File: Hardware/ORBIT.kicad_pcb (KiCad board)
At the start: 2 copper layers, 50 x 50 mm, 53 parts, among them J1 West Connector, J2 East Connector, U1 MCP73031, U10 8MHz, U11 30p, U12 30p, U13 22uF, U14 10uF, U15 TPS63802DLAR, U16 STM32F030C8Tx, U17 AT24C128C, U18 10p, U19 100n, U2 4u7, U20 4.7uF, U21 100nF, U22 CP2102-GMR, U23 1uF, U24 100nF, U3 100n, U4 100n, U5 100n, U6 100n, U7 4u7, U8 4u7, U9 100n

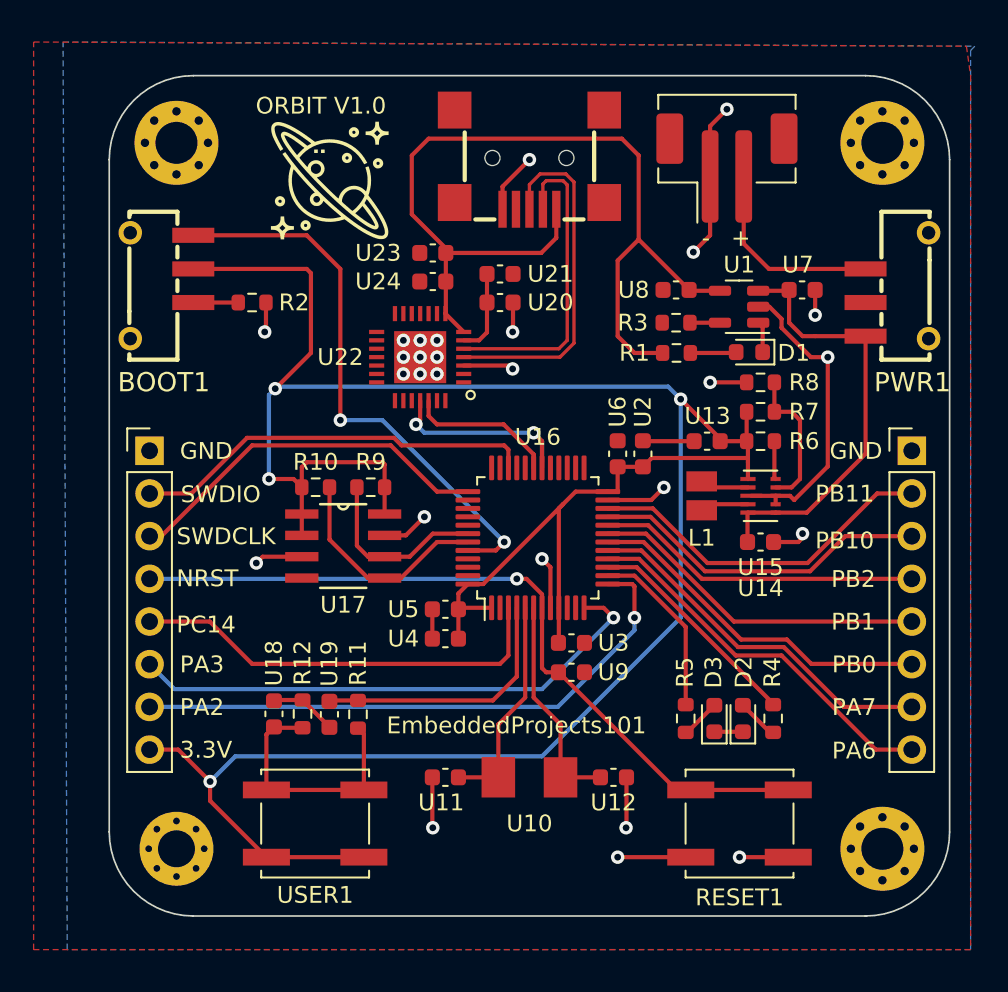
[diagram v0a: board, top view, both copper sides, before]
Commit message: all components in the final positioned
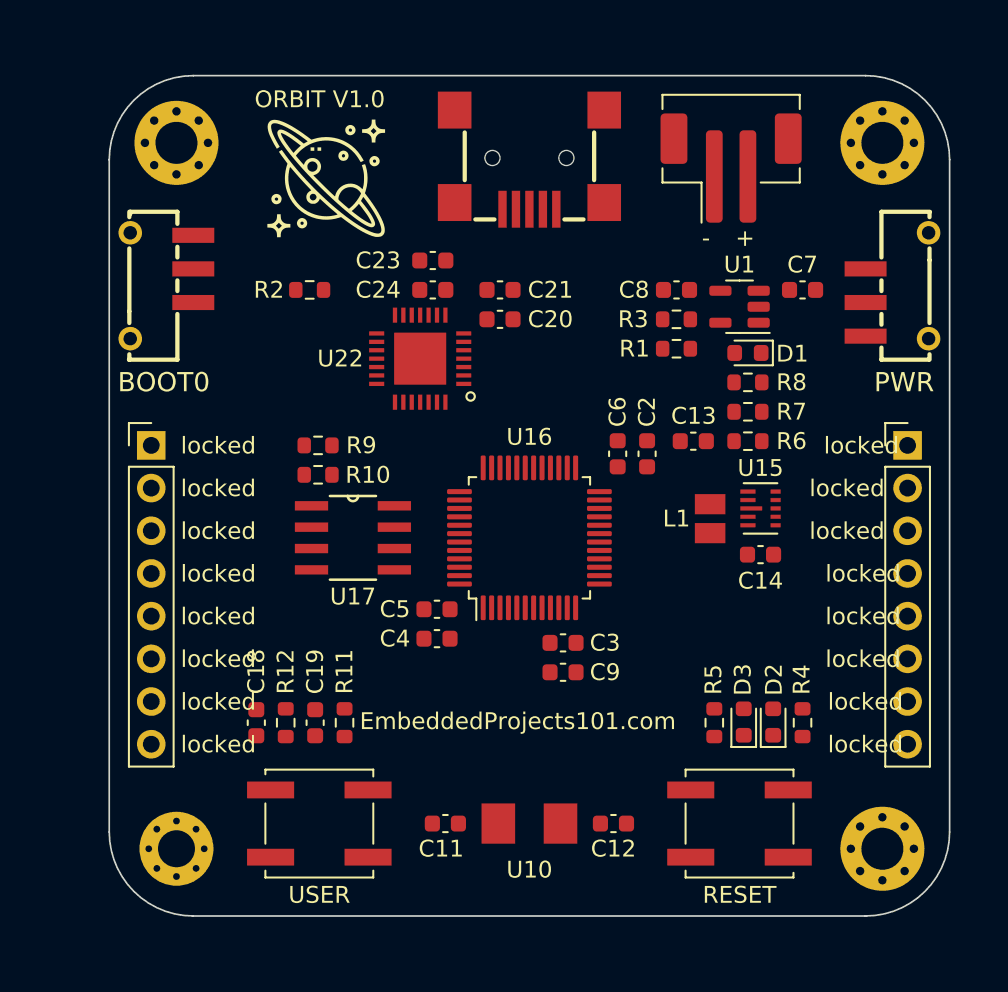
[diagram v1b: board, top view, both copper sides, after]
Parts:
- moved R9 4.00 mm to (136.4, 92.0), turned to 180 degrees
- moved R2 3.51 mm to (135.9, 82.8)
- moved C11 2.75 mm to (144.0, 114.5)
- moved C12 2.75 mm to (154.0, 114.5)
- moved U10 2.75 mm to (149.0, 114.5)
- moved D2 1.81 mm to (163.5, 108.5)
- moved R4 1.77 mm to (165.2, 108.5)
- moved D3 1.76 mm to (161.8, 108.5)
- moved R5 1.72 mm to (160.0, 108.5)
- moved L1 1.45 mm to (159.8, 96.4)
- moved C18 1.17 mm to (132.8, 108.5)
- moved R12 1.13 mm to (134.5, 108.5)
- moved C20 1.00 mm to (147.2, 84.5)
- moved C19 0.99 mm to (136.2, 108.5)
- moved C21 0.95 mm to (147.2, 82.8)
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- renumbered BOOT1 to BOOT0, U11 to C11, U12 to C12, U13 to C13, U14 to C14, U18 to C18, U19 to C19, U2 to C2, U20 to C20, U21 to C21, U23 to C23, U24 to C24, U3 to C3, U4 to C4, U5 to C5, U6 to C6, U7 to C7, U8 to C8, U9 to C9, PWR1 to PWR, RESET1 to RESET, USER1 to USER
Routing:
- net +3.3V: track 163.8 -> 0.00 mm, vias 4 -> 0
- net GND: track 79.6 -> 0.00 mm, vias 27 -> 0
- net VBUS: track 55.2 -> 0.00 mm
- net NRST: track 45.8 -> 0.00 mm, vias 1 -> 0
- net PA3: track 35.0 -> 0.00 mm, vias 1 -> 0
- net Net-(U16-BOOT0): track 33.7 -> 0.00 mm, vias 2 -> 0
- net PA2: track 32.0 -> 0.00 mm, vias 1 -> 0
- net +BATT: track 25.9 -> 0.00 mm
- net PC14: track 25.4 -> 0.00 mm
- net SWDIO: track 24.1 -> 0.00 mm
- net PA6: track 22.8 -> 0.00 mm
- net SWDCLK: track 22.3 -> 0.00 mm
- net PA7: track 21.9 -> 0.00 mm
- net PB11: track 21.1 -> 0.00 mm
- net PB0: track 21.1 -> 0.00 mm
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- removed copper zone on B.Cu, net GND
- removed copper zone on F.Cu, net GND
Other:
- board text added: "EmbeddedProjects101.com"
- board text added: "locked"
- board text removed: "3.3V"
- board text removed: "EmbeddedProjects101"
- board text removed: "GND"
- board text removed: "NRST"
- board text removed: "PA2"
- board text removed: "PA3"
- board text removed: "PA6"
- board text removed: "PA7"
- board text removed: "PB0"
- board text removed: "PB1"
- board text removed: "PB10"
- board text removed: "PB11"
- board text removed: "PB2"
- board text removed: "PC14"
- board text removed: "SWDCLK"
- board text removed: "SWDIO"

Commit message: Version 1.0
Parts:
- PWR1: renamed from PWR; value PWR_SW -> PWR
- SW1: renamed from RESET; value SW_Push -> RESET
- SW2: renamed from USER; value SW_Push -> USER
- moved R2 3.02 mm to (133.0, 83.5)
- renumbered G*** to O
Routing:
- net +3.3V: track 0.00 -> 167.7 mm, vias 0 -> 4
- net VBUS: track 0.00 -> 56.8 mm
- net NRST: track 0.00 -> 50.2 mm, vias 0 -> 2
- net Net-(U16-BOOT0): track 0.00 -> 47.1 mm, vias 0 -> 2
- net PA3: track 0.00 -> 35.7 mm, vias 0 -> 2
- net PA2: track 0.00 -> 31.4 mm, vias 0 -> 2
- net +BATT: track 0.00 -> 25.3 mm
- net PC14: track 0.00 -> 24.7 mm
- net SWDIO: track 0.00 -> 24.4 mm, vias 0 -> 2
- net PB11: track 0.00 -> 23.0 mm
- net PA6: track 0.00 -> 22.9 mm
- net PB10: track 0.00 -> 22.1 mm
- net PA7: track 0.00 -> 22.1 mm
- net GND: track 0.00 -> 21.9 mm, vias 0 -> 31
- net PB2: track 0.00 -> 21.4 mm
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- added copper zone on B.Cu, net GND
- added copper zone on F.Cu, net GND
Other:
- board text added: "3.3V"
- board text added: "GND"
- board text added: "NRST"
- board text added: "PA2"
- board text added: "PA3"
- board text added: "PA6"
- board text added: "PA7"
- board text added: "PB0"
- board text added: "PB1"
- board text added: "PB10"
- board text added: "PB11"
- board text added: "PB2"
- board text added: "PC14"
- board text added: "SWDCLK"
- board text added: "SWDIO"
- board text removed: "locked"
